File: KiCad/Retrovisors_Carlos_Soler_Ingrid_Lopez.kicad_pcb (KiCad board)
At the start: 2 copper layers, 125.5 x 100.5 mm, 121 parts, among them IC1 PIC24H, J1 Conn_01x02, J11 Conn_01x02, J12 Conn_01x02, J14 Conn_01x02_Pin, J2 DE9_Plug_MountingHoles, J3 DE9_Plug_MountingHoles, J3-4 Conn_01x02, J4 Conn_01x03, J5 Conn_01x02, J7 Conn_01x05, J7-8 Conn_01x02, J9 Conn_01x02, K1 G6E, K10 G6E, K2 G6E, K3 G6E, K4 G6E, K5 G6E, K6 G6E, K7 G6E, K8 G6E, K9 G6E, Q1 NMOS, Q10 NMOS, Q11 IRLZ44N, Q12 IRLZ44N, Q2 NMOS, Q3 NMOS, Q4 NMOS, Q5 NMOS, Q6 NMOS, Q7 NMOS, Q8 NMOS, Q9 NMOS, SW1 SW_DP3T, SW2 SW_DP3T, SW3 SW_DP3T, SW4 OP/CL, SW7 OP/CL, U1 TSR0.5-2450, U2 MCP2551-I-SN, U4 type="X" model="OPAMP" lib="", U5 type="X" model="OPAMP" lib="", U6 LM1117DT-3.3, Y1 Crystal

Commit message: prueba para unir a la main
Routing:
- net GND: track 7.82 -> 19.9 mm, vias 29 -> 35
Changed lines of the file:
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@@
+	)
+	(segment
+		(start 87.55 74.1)
+		(end 87.65 74.2)
+		(width 0.2)
+		(layer "F.Cu")
+		(net 1)
+	)
+	(segment
+		(start 86 82.9)
+		(end 88.1 82.9)
+		(width 0.2)
+		(layer "F.Cu")
+		(net 1)
 	)
 	(segment
@@
 	)
 	(segment
+		(start 87.75 59.45)
+		(end 87.85 59.55)
+		(width 0.2)
+		(layer "F.Cu")
+		(net 1)
+	)
+	(segment
 		(start 128.8108 112.7329)
 		(end 128.8108 110.9217)
@@
 	)
 	(segment
+		(start 83.9 74.1)
+		(end 83.8 74.2)
+		(width 0.2)
+		(layer "F.Cu")
+		(net 1)
+	)
+	(segment
+		(start 85.7 74.1)
+		(end 83.9 74.1)
+		(width 0.2)
+		(layer "F.Cu")
+		(net 1)
+	)
+	(segment
 		(start 128.8108 107.1449)
 		(end 128.8108 108.7783)
@@
 		(net 1)
 	)
+	(segment
+		(start 88.1 82.9)
+		(end 88.15 82.95)
+		(width 0.2)
+		(layer "F.Cu")
+		(net 1)
+	)
+	(segment
+		(start 84.05 82.9)
+		(end 86 82.9)
+		(width 0.2)
+		(layer "F.Cu")
+		(net 1)
+	)
+	(segment
+		(start 85.65 59.55)
+		(end 85.75 59.45)
+		(width 0.2)
+		(layer "F.Cu")
+		(net 1)
+	)
+	(segment
+		(start 83.9 59.55)
+		(end 85.65 59.55)
+		(width 0.2)
+		(layer "F.Cu")
+		(net 1)
+	)
+	(segment
+		(start 85.7 74.1)
+		(end 87.55 74.1)
+		(width 0.2)
+		(layer "F.Cu")
+		(net 1)
+	)
+	(segment
+		(start 85.75 59.45)
+		(end 87.75 59.45)
+		(width 0.2)
+		(layer "F.Cu")
+		(net 1)
+	)
+	(via
+		(at 84.05 82.9)
+		(size 0.6)
+		(drill 0.3)
+		(layers "F.Cu" "B.Cu")
+		(free yes)
+		(net 1)
+	)
 	(via
 		(at 127.66 104.9919)
@@
 	)
 	(via
+		(at 83.9 59.55)
+		(size 0.6)
+		(drill 0.3)
+		(layers "F.Cu" "B.Cu")
+		(free yes)
+		(net 1)
+	)
+	(via
+		(at 87.85 59.55)
+		(size 0.6)
+		(drill 0.3)
+		(layers "F.Cu" "B.Cu")
+		(free yes)
+		(net 1)
+	)
+	(via
 		(at 134.01 104.4525)
 		(size 0.8)
@@
 	)
 	(via
+		(at 87.65 74.2)
+		(size 0.6)
+		(drill 0.3)
+		(layers "F.Cu" "B.Cu")
+		(free yes)
+		(net 1)
+	)
+	(via
 		(at 132.74 104.4525)
 		(size 0.8)
@@
 		(layers "F.Cu" "B.Cu")
 		(free yes)
+		(net 1)
+	)
+	(via
+		(at 88.15 82.95)
+		(size 0.6)
+		(drill 0.3)
+		(layers "F.Cu" "B.Cu")
+		(free yes)
+		(net 1)
+	)
+	(via
+		(at 83.8 74.2)
+		(size 0.6)
+		(drill 0.3)
+		(layers "F.Cu" "B.Cu")
+		(free yes)

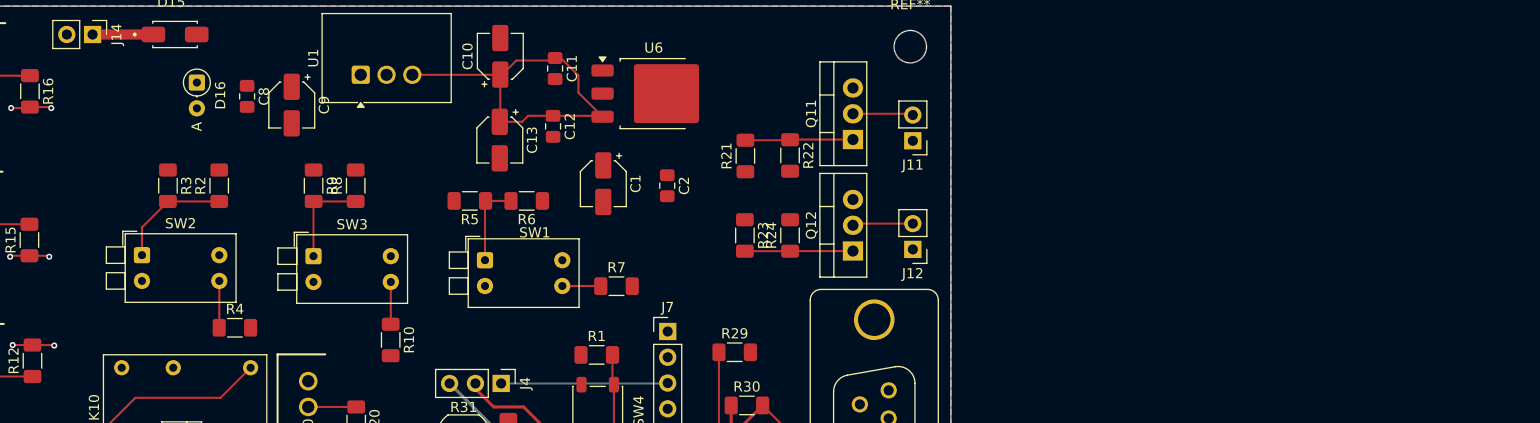
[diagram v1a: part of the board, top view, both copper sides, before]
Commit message: modificando todos los GND eliminamos GND PWR
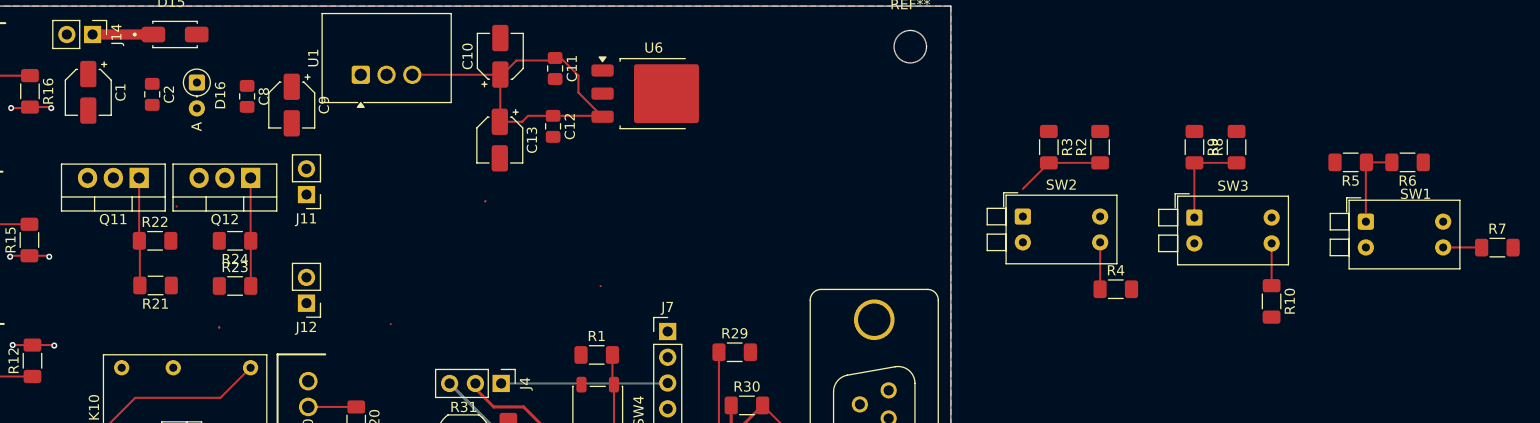
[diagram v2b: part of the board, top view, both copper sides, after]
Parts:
- moved R3 86.9 mm to (186.2, 63.4)
- moved R5 86.9 mm to (215.9, 64.9)
- moved R6 86.9 mm to (221.5, 64.9)
- moved R8 86.9 mm to (204.7, 63.4)
- moved SW3 86.9 mm to (200.5, 70.3)
- moved R10 86.9 mm to (208.1, 78.6)
- moved R4 86.9 mm to (192.8, 77.4)
- moved R9 86.9 mm to (200.5, 63.4)
- moved SW2 86.9 mm to (183.6, 70.2)
- moved R2 86.9 mm to (191.2, 63.4)
- moved R7 86.9 mm to (230.3, 73.3)
- moved SW1 86.9 mm to (217.4, 70.7)
- moved Q11 70.4 mm to (96.5, 66.4), turned to 180 degrees
- moved R22 63.1 mm to (98.1, 72.6), turned to 0 degrees
- moved J11 60.0 mm to (113.0, 68.1)
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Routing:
- net Net-(J11-Pin_2): track 5.95 -> 0.18 mm
- net Net-(J12-Pin_2): track 5.97 -> 0.28 mm
- net Net-(R2-Pad1): track 11.4 -> 8.67 mm

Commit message: millora de placement
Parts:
- moved R9 98.2 mm to (133.5, 135.2), turned to 90 degrees
- moved SW1 97.7 mm to (153.3, 144.5), turned to 90 degrees
- moved R8 96.6 mm to (133.3, 128.6)
- moved SW3 96.2 mm to (139.1, 144.4), turned to 90 degrees
- moved R7 94.9 mm to (156.2, 132.5), turned to 180 degrees
- moved SW2 93.8 mm to (126.1, 144.4), turned to 90 degrees
- moved R3 92.5 mm to (123.5, 131.3), turned to 90 degrees
- moved R2 91.7 mm to (123.5, 125.2)
- moved R6 89.0 mm to (157.7, 126.9), turned to 90 degrees
- moved R4 84.1 mm to (128.6, 131.8)
- moved C7 82.3 mm to (169.0, 62.8), turned to 0 degrees
- moved R10 81.7 mm to (146.6, 132.3), turned to 0 degrees
- moved R5 80.6 mm to (157.7, 120.5), turned to 90 degrees
- moved R25 79.6 mm to (168.9, 66.3), turned to 0 degrees
- moved D1 77.4 mm to (168.9, 69.7)
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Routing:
- net FI_MOTOR: track 47.5 -> 1.63 mm, vias 1 -> 0
- net Net-(U5-+): track 22.9 -> 0.00 mm, vias 2 -> 0
- net /TX: track 24.6 -> 4.87 mm
- net /RX: track 24.0 -> 7.31 mm
- net angle_m: track 13.8 -> 0.95 mm
- net Net-(R8-Pad1): track 9.55 -> 0.01 mm
- net Net-(U4--): track 9.37 -> 0.00 mm
- net Net-(U5-V-): track 9.30 -> 0.00 mm
- net Net-(U5--): track 9.25 -> 0.00 mm
- net Net-(R2-Pad1): track 8.67 -> 0.00 mm
- net Net-(R5-Pad1): track 8.37 -> 0.08 mm
- net Net-(U4-+): track 7.26 -> 0.04 mm
- net /CAN+: track 19.1 -> 24.4 mm
- net /CAN-: track 21.6 -> 16.3 mm
- net Net-(R37-Pad1): track 5.11 -> 0.00 mm
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
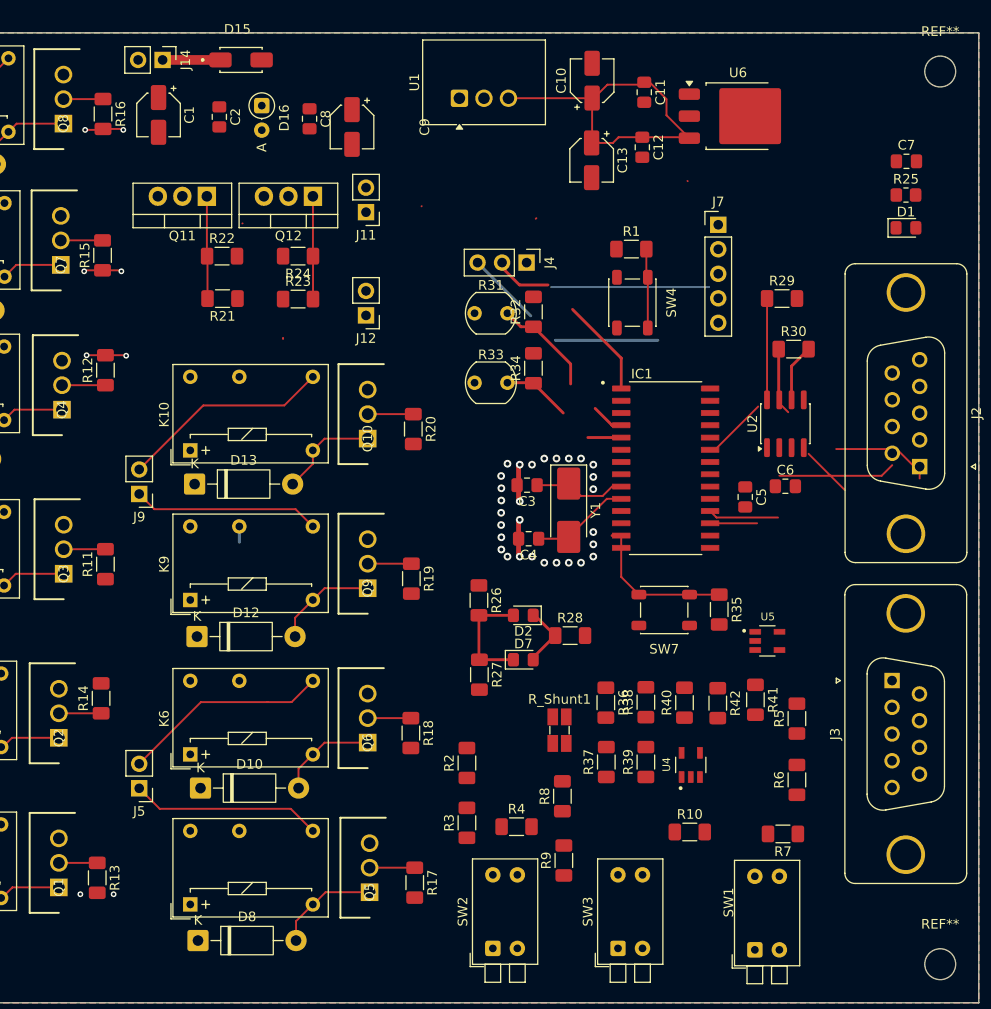
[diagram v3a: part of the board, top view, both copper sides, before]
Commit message: Enrotament Part digital finalitzada
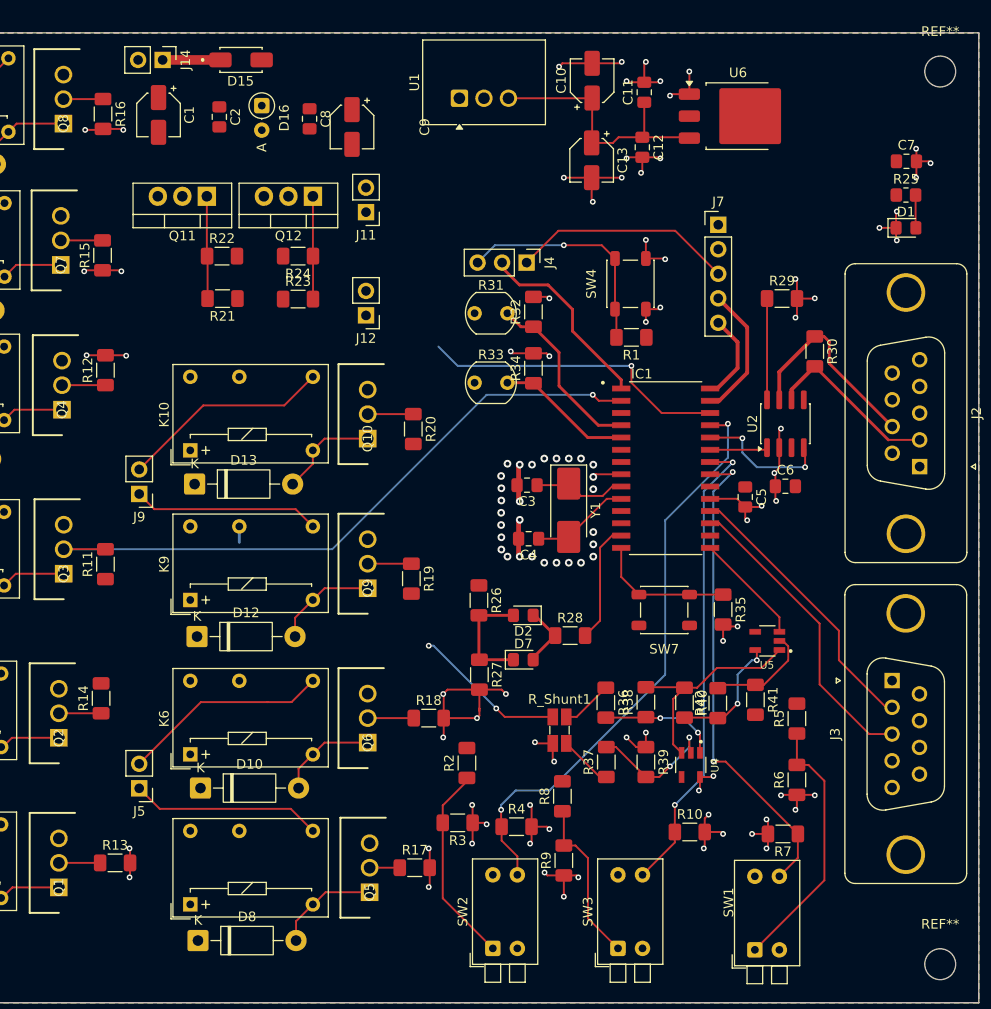
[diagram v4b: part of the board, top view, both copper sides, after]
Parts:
- moved R1 9.15 mm to (140.5, 81.0), turned to 180 degrees
- moved R13 2.41 mm to (87.0, 135.5), turned to 0 degrees
- moved R18 2.41 mm to (119.5, 120.5), turned to 0 degrees
- moved R30 2.20 mm to (159.5, 82.5), turned to -90 degrees
- moved SW4 1.96 mm to (140.4, 75.5), turned to 90 degrees
- moved R17 1.55 mm to (118.0, 136.0), turned to 0 degrees
- moved R3 0.96 mm to (122.5, 131.3), turned to 180 degrees
- moved R35 0.40 mm to (150.0, 109.2)
- turned C11 to 90 degrees
- turned R39 to -90 degrees
- turned R40 to -90 degrees
- turned R42 to 90 degrees
- turned U4 to -90 degrees
- turned U5 to 180 degrees
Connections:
- net /CAN+ renamed /Digital/CAN+
- net /CAN- renamed /Digital/CAN-
- net /RX renamed /Digital/RX
- net /TX renamed /Digital/TX
- net /Vdrain1 renamed /Poténcia/Vdrain1
- net /Vdrain3 renamed /Poténcia/Vdrain3
- net /Vdrain4 renamed /Poténcia/Vdrain4
- net Net-(R36-Pad1) renamed /Poténcia/Shunt2
- net Net-(R37-Pad1) renamed /Poténcia/Shunt3
- net Net-(U4-+) renamed /Poténcia/V+
- net Net-(U4--) renamed /Poténcia/V-
- C8 pad 2: GNDPWR -> GND
- C9 pad 2: GNDPWR -> GND
- D10 pad 2: /Vdrain2 -> unconnected-(D10-A-Pad2)
- D13 pad 2: /Vdrain2 -> /Poténcia/Vdrain2
- D16 pad 2: GNDPWR -> GND
- D6 pad 2: /Vdrain2 -> /Poténcia/Vdrain2
- J14 pad 2: GNDPWR -> GND
- K1 pad 10: GNDPWR -> GND
- K10 pad 6: /Vdrain2 -> /Poténcia/Vdrain2
- K2 pad 10: GNDPWR -> GND
- K2 pad 6: /Vdrain2 -> /Poténcia/Vdrain2
- K3 pad 10: GNDPWR -> GND
- K4 pad 10: GNDPWR -> GND
- K5 pad 10: GNDPWR -> GND
- K6 pad 10: GNDPWR -> GND
- K6 pad 6: /Vdrain2 -> unconnected-(K6-Pad6)
- K7 pad 10: GNDPWR -> GND
- K8 pad 10: GNDPWR -> GND
- Q1 pad 3: GNDPWR -> GND
- Q10 pad 1: /Vdrain2 -> /Poténcia/Vdrain2
- Q10 pad 3: GNDPWR -> GND
- Q2 pad 1: /Vdrain2 -> /Poténcia/Vdrain2
- Q2 pad 3: GNDPWR -> GND
- Q3 pad 3: GNDPWR -> GND
- Q4 pad 3: GNDPWR -> GND
- Q5 pad 3: GNDPWR -> GND
- Q6 pad 1: /Vdrain2 -> unconnected-(Q6-D-Pad1)
- Q6 pad 3: GNDPWR -> GND
- Q7 pad 3: GNDPWR -> GND
- Q8 pad 3: GNDPWR -> GND
- Q9 pad 3: GNDPWR -> GND
- U1 pad 2: GNDPWR -> GND
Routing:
- net GND: track 19.9 -> 169.7 mm, vias 35 -> 103
- net DLY_U: track 4.33 -> 69.0 mm, vias 0 -> 1
- net LM_button: track 0.06 -> 61.1 mm, vias 0 -> 2
- net RM_button: track 0.02 -> 50.3 mm, vias 0 -> 2
- net select_button: track 0.01 -> 49.0 mm, vias 0 -> 2
- net CAL_L: track 0.00 -> 32.0 mm, vias 0 -> 1
- net /Vdrain2: track 31.9 -> 0.00 mm
- net Net-(R5-Pad1): track 0.08 -> 27.3 mm
- net /Digital/TX: track 4.87 -> 31.6 mm
- net Net-(U5-+): track 0.00 -> 23.2 mm
- net /Digital/RX: track 7.31 -> 29.1 mm
- net /Poténcia/Vdrain2: track 0.00 -> 21.6 mm
- net Net-(R2-Pad1): track 0.00 -> 20.8 mm
- net Net-(R8-Pad1): track 0.01 -> 17.3 mm
- net FI_MOTOR: track 1.63 -> 17.5 mm, vias 0 -> 2
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
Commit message: canvis en el readme, a més de petites modificacions de PCB part digital
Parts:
- J2, J3: footprint AA_footprints:DSUB-9_Female_Vertical_Pitch2.77x2.84mm_MountingHoles -> Connector_Dsub:DSUB-9_Pins_Horizontal_P2.77x2.54mm_EdgePinOffset9.40mm
- moved J3 10.7 mm to (163.5, 126.5)
- moved J2 7.69 mm to (163.5, 91.0), turned to 90 degrees
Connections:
- net Net-(IC1-OSC1/CLKI/RA7) renamed /Digital/OSC1
- net Net-(IC1-OSC2/CLKO/RA6) renamed /Digital/OSC2
- IC1 pad 17: /Digital/TX -> /Digital/RX
- IC1 pad 18: /Digital/RX -> /Digital/TX
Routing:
- net CAL_R: track 0.00 -> 9.68 mm, vias 0 -> 1
- net /Digital/CAN-: track 18.5 -> 10.3 mm
- net /Digital/CAN+: track 21.7 -> 18.0 mm
- net /Digital/TX: track 31.6 -> 29.2 mm
- net /Digital/RX: track 29.1 -> 30.2 mm
